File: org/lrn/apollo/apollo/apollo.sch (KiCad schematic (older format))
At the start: 2 parts, among them U1 74HC595, U2 5461AS-1

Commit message: apollo pcb
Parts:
- added J1, J2, J3, J4, J_CLK1, J_CLR1, J_GND1, J_OE1, J_SER1, J_VCC1: Conn_01x01_Male, Connector_Pin:Pin_D0.7mm_L6.5mm_W1.8mm_FlatFork, symbol Connector:Conn_01x01_Male
- added Q1, Q2, Q3, Q4: PN2222A, Package_TO_SOT_THT:TO-92_Inline, symbol Transistor_BJT:PN2222A
- added R1, R2, R3, R4, R5, R6, R7, R8: R, Resistor_THT:R_Axial_DIN0204_L3.6mm_D1.6mm_P5.08mm_Horizontal, symbol Device:R
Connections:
- net at U2.1 (es): now also R3.1; no longer U1.4 (QE)
- net at U2.10 (fs): now also R7.1; no longer U1.5 (QF)
- net at U2.11 (as): now also R1.1; no longer U1.15 (QA)
- net at U2.12 (d1): now also Q2.3 (C)
- net at U2.2 (ds): now also R6.1; no longer U1.3 (QD)
- net at U2.3 (dps): now also R8.1; no longer U1.7 (QH)
- net at U2.4 (cs): now also R2.1; no longer U1.2 (QC)
- net at U2.5 (gs): now also R4.1; no longer U1.6 (QG)
- net at U2.6 (d4): now also Q1.3 (C)
- net at U2.7 (bs): now also R5.1; no longer U1.1 (QB)
- net at U2.8 (d3): now also Q4.3 (C)
- net at U2.9 (d2): now also Q3.3 (C)
- net at U1.10 (~SRCLR): now also U1.16 (VCC), J_VCC1.1 (Pin_1)
- net at U1.11 (SRCLK): now also J_CLR1.1 (Pin_1)
- net at U1.12 (RCLK): now also J_CLK1.1 (Pin_1)
- net at U1.13 (~OE): now also J_OE1.1 (Pin_1)
- net at U1.14 (SER): now also J_SER1.1 (Pin_1)
- net at U1.8 (GND): now also J_GND1.1 (Pin_1), Q1.1 (E), Q2.1 (E), Q3.1 (E), Q4.1 (E)
- new net: R5.2, U1.1 (QB)
- new net: R1.2, U1.15 (QA)
- new net: R2.2, U1.2 (QC)
- new net: R6.2, U1.3 (QD)
- new net: R3.2, U1.4 (QE)
- new net: R7.2, U1.5 (QF)
- new net: R4.2, U1.6 (QG)
- new net: R8.2, U1.7 (QH)
- new net: J2.1 (Pin_1), Q2.2 (B)
- new net: J3.1 (Pin_1), Q3.2 (B)
- new net: J4.1 (Pin_1), Q4.2 (B)
- new net: J1.1 (Pin_1), Q1.2 (B)
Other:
- moved on the sheet: U1, U2

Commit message: apollo pcb fix: wrong transistor footprint
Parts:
- Q1, Q2, Q3, Q4: footprint Package_TO_SOT_THT:TO-92_Inline -> Package_TO_SOT_THT:TO-92_Wide
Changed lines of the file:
@@
 F 0 "Q2" H 5390 2096 50  0000 L CNN
 F 1 "PN2222A" H 5390 2005 50  0000 L CNN
-F 2 "Package_TO_SOT_THT:TO-92_Inline" H 5400 1975 50  0001 L CIN
+F 2 "Package_TO_SOT_THT:TO-92_Wide" H 5400 1975 50  0001 L CIN
 F 3 "http://www.fairchildsemi.com/ds/PN/PN2222A.pdf" H 5200 2050 50  0001 L CNN
 	1    5200 2050
@@
 F 0 "Q3" H 5740 2696 50  0000 L CNN
 F 1 "PN2222A" H 5740 2605 50  0000 L CNN
-F 2 "Package_TO_SOT_THT:TO-92_Inline" H 5750 2575 50  0001 L CIN
+F 2 "Package_TO_SOT_THT:TO-92_Wide" H 5750 2575 50  0001 L CIN
 F 3 "http://www.fairchildsemi.com/ds/PN/PN2222A.pdf" H 5550 2650 50  0001 L CNN
 	1    5550 2650
@@
 F 0 "Q4" H 6090 3196 50  0000 L CNN
 F 1 "PN2222A" H 6090 3105 50  0000 L CNN
-F 2 "Package_TO_SOT_THT:TO-92_Inline" H 6100 3075 50  0001 L CIN
+F 2 "Package_TO_SOT_THT:TO-92_Wide" H 6100 3075 50  0001 L CIN
 F 3 "http://www.fairchildsemi.com/ds/PN/PN2222A.pdf" H 5900 3150 50  0001 L CNN
 	1    5900 3150
@@
 F 0 "Q1" H 5040 1546 50  0000 L CNN
 F 1 "PN2222A" H 5040 1455 50  0000 L CNN
-F 2 "Package_TO_SOT_THT:TO-92_Inline" H 5050 1425 50  0001 L CIN
+F 2 "Package_TO_SOT_THT:TO-92_Wide" H 5050 1425 50  0001 L CIN
 F 3 "http://www.fairchildsemi.com/ds/PN/PN2222A.pdf" H 4850 1500 50  0001 L CNN
 	1    4850 1500

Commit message: apollo: new pcb
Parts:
- added Rb1, Rb2, Rb3, Rb4: R, apollo:R__Horizontal, symbol Device:R
- Q1, Q2, Q3, Q4: footprint Package_TO_SOT_THT:TO-92_Wide -> apollo:2N222A-TO-92_Wide
- R1, R2, R3, R4, R5, R6, R7, R8: footprint Resistor_THT:R_Axial_DIN0204_L3.6mm_D1.6mm_P5.08mm_Horizontal -> apollo:R__Horizontal
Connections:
- net VCC: now reaches J_VCC1.1 (Pin_1), U1.10 (~SRCLR), U1.16 (VCC)
- net GND: now reaches J_GND1.1 (Pin_1), Q1.1 (E), Q2.1 (E), Q3.1 (E), Q4.1 (E), U1.8 (GND)
- net at Q2.2 (B): now also Rb2.1; no longer J2.1 (Pin_1)
- net at Q3.2 (B): now also Rb3.1; no longer J3.1 (Pin_1)
- net at Q4.2 (B): now also Rb4.1; no longer J4.1 (Pin_1)
- net at Q1.2 (B): now also Rb1.1; no longer J1.1 (Pin_1)
- new net: J4.1 (Pin_1), Rb4.2
- new net: J3.1 (Pin_1), Rb3.2
- new net: J2.1 (Pin_1), Rb2.2
- new net: J1.1 (Pin_1), Rb1.2
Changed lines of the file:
@@
 F 0 "R7" V 4400 5050 50  0000 C CNN
 F 1 "R" V 4400 4950 50  0000 C CNN
-F 2 "Resistor_THT:R_Axial_DIN0204_L3.6mm_D1.6mm_P5.08mm_Horizontal" V 4330 5000 50  0001 C CNN
+F 2 "apollo:R__Horizontal" V 4330 5000 50  0001 C CNN
 F 3 "~" H 4400 5000 50  0001 C CNN
 	1    4400 5000
@@
 F 0 "R5" V 4400 4650 50  0000 C CNN
 F 1 "R" V 4400 4550 50  0000 C CNN
-F 2 "Resistor_THT:R_Axial_DIN0204_L3.6mm_D1.6mm_P5.08mm_Horizontal" V 4330 4600 50  0001 C CNN
+F 2 "apollo:R__Horizontal" V 4330 4600 50  0001 C CNN
 F 3 "~" H 4400 4600 50  0001 C CNN
 	1    4400 4600
@@
 F 0 "R2" V 4150 4750 50  0000 C CNN
 F 1 "R" V 4150 4650 50  0000 C CNN
-F 2 "Resistor_THT:R_Axial_DIN0204_L3.6mm_D1.6mm_P5.08mm_Horizontal" V 4080 4700 50  0001 C CNN
+F 2 "apollo:R__Horizontal" V 4080 4700 50  0001 C CNN
 F 3 "~" H 4150 4700 50  0001 C CNN
 	1    4150 4700
@@
 F 0 "R1" V 4150 4550 50  0000 C CNN
 F 1 "R" V 4150 4450 50  0000 C CNN
-F 2 "Resistor_THT:R_Axial_DIN0204_L3.6mm_D1.6mm_P5.08mm_Horizontal" V 4080 4500 50  0001 C CNN
+F 2 "apollo:R__Horizontal" V 4080 4500 50  0001 C CNN
 F 3 "~" H 4150 4500 50  0001 C CNN
 	1    4150 4500
@@
 F 0 "R6" V 4400 4850 50  0000 C CNN
 F 1 "R" V 4400 4750 50  0000 C CNN
-F 2 "Resistor_THT:R_Axial_DIN0204_L3.6mm_D1.6mm_P5.08mm_Horizontal" V 4330 4800 50  0001 C CNN
+F 2 "apollo:R__Horizontal" V 4330 4800 50  0001 C CNN
 F 3 "~" H 4400 4800 50  0001 C CNN
 	1    4400 4800
@@
 F 0 "R3" V 4150 4950 50  0000 C CNN
 F 1 "R" V 4150 4850 50  0000 C CNN
-F 2 "Resistor_THT:R_Axial_DIN0204_L3.6mm_D1.6mm_P5.08mm_Horizontal" V 4080 4900 50  0001 C CNN
+F 2 "apollo:R__Horizontal" V 4080 4900 50  0001 C CNN
 F 3 "~" H 4150 4900 50  0001 C CNN
 	1    4150 4900
@@
 F 0 "R4" V 4150 5150 50  0000 C CNN
 F 1 "R" V 4150 5050 50  0000 C CNN
-F 2 "Resistor_THT:R_Axial_DIN0204_L3.6mm_D1.6mm_P5.08mm_Horizontal" V 4080 5100 50  0001 C CNN
+F 2 "apollo:R__Horizontal" V 4080 5100 50  0001 C CNN
 F 3 "~" H 4150 5100 50  0001 C CNN
 	1    4150 5100
@@
 F 0 "R8" V 4400 5250 50  0000 C CNN
 F 1 "R" V 4400 5150 50  0000 C CNN
-F 2 "Resistor_THT:R_Axial_DIN0204_L3.6mm_D1.6mm_P5.08mm_Horizontal" V 4330 5200 50  0001 C CNN
+F 2 "apollo:R__Horizontal" V 4330 5200 50  0001 C CNN
 F 3 "~" H 4400 5200 50  0001 C CNN
 	1    4400 5200
@@
 F 0 "Q2" H 5390 2096 50  0000 L CNN
 F 1 "PN2222A" H 5390 2005 50  0000 L CNN
-F 2 "Package_TO_SOT_THT:TO-92_Wide" H 5400 1975 50  0001 L CIN
+F 2 "apollo:2N222A-TO-92_Wide" H 5400 1975 50  0001 L CIN
 F 3 "http://www.fairchildsemi.com/ds/PN/PN2222A.pdf" H 5200 2050 50  0001 L CNN
 	1    5200 2050
@@
 F 0 "Q3" H 5740 2696 50  0000 L CNN
 F 1 "PN2222A" H 5740 2605 50  0000 L CNN
-F 2 "Package_TO_SOT_THT:TO-92_Wide" H 5750 2575 50  0001 L CIN
+F 2 "apollo:2N222A-TO-92_Wide" H 5750 2575 50  0001 L CIN
 F 3 "http://www.fairchildsemi.com/ds/PN/PN2222A.pdf" H 5550 2650 50  0001 L CNN
 	1    5550 2650
@@
 F 0 "Q4" H 6090 3196 50  0000 L CNN
 F 1 "PN2222A" H 6090 3105 50  0000 L CNN
-F 2 "Package_TO_SOT_THT:TO-92_Wide" H 6100 3075 50  0001 L CIN
+F 2 "apollo:2N222A-TO-92_Wide" H 6100 3075 50  0001 L CIN
 F 3 "http://www.fairchildsemi.com/ds/PN/PN2222A.pdf" H 5900 3150 50  0001 L CNN
 	1    5900 3150
@@
 F 0 "Q1" H 5040 1546 50  0000 L CNN
 F 1 "PN2222A" H 5040 1455 50  0000 L CNN
-F 2 "Package_TO_SOT_THT:TO-92_Wide" H 5050 1425 50  0001 L CIN
+F 2 "apollo:2N222A-TO-92_Wide" H 5050 1425 50  0001 L CIN
 F 3 "http://www.fairchildsemi.com/ds/PN/PN2222A.pdf" H 4850 1500 50  0001 L CNN
 	1    4850 1500
@@
 	1    0    0    -1
 $EndComp
-Wire Wire Line
-	5350 2650 2750 2650
 $Comp
 L Connector:Conn_01x01_Male J2
@@
 	1    0    0    -1
 $EndComp
-Wire Wire Line
-	2750 2050 5000 2050
 $Comp
 L Connector:Conn_01x01_Male J1
@@
 	1    0    0    -1
 $EndComp
-Wire Wire Line
-	2750 1500 4650 1500
 Connection ~ 4150 3700
 Wire Wire Line
@@
 $EndComp
 Wire Wire Line
-	5700 3150 2750 3150
-Wire Wire Line
 	2750 5000 3100 5000
 Wire Wire Line
 	5600 3800 5600 4400
+$Comp
+L Device:R Rb1
+U 1 1 5F5EB03E
+P 3750 1500
+F 0 "Rb1" V 3543 1500 50  0000 C CNN
+F 1 "R" V 3634 1500 50  0000 C CNN
+F 2 "apollo:R__Horizontal" V 3680 1500 50  0001 C CNN
+F 3 "~" H 3750 1500 50  0001 C CNN
+	1    3750 1500
+	0    1    1    0
+$EndComp
+$Comp
+L Device:R Rb2
+U 1 1 5F5EB7B3
+P 3750 2050
+F 0 "Rb2" V 3543 2050 50  0000 C CNN
+F 1 "R" V 3634 2050 50  0000 C CNN
+F 2 "apollo:R__Horizontal" V 3680 2050 50  0001 C CNN
+F 3 "~" H 3750 2050 50  0001 C CNN
+	1    3750 2050
+	0    1    1    0
+$EndComp
+$Comp
+L Device:R Rb3
+U 1 1 5F5EBD6A
+P 3750 2650
+F 0 "Rb3" V 3543 2650 50  0000 C CNN
+F 1 "R" V 3634 2650 50  0000 C CNN
+F 2 "apollo:R__Horizontal" V 3680 2650 50  0001 C CNN
+F 3 "~" H 3750 2650 50  0001 C CNN
+	1    3750 2650
+	0    1    1    0
+$EndComp
+$Comp
+L Device:R Rb4
+U 1 1 5F5EC2EE
+P 3750 3150
+F 0 "Rb4" V 3543 3150 50  0000 C CNN
+F 1 "R" V 3634 3150 50  0000 C CNN
+F 2 "apollo:R__Horizontal" V 3680 3150 50  0001 C CNN
+F 3 "~" H 3750 3150 50  0001 C CNN
+	1    3750 3150
+	0    1    1    0
+$EndComp
+Wire Wire Line
+	2750 3150 3600 3150
+Wire Wire Line
+	2750 2650 3600 2650
+Wire Wire Line
+	2750 2050 3600 2050
+Wire Wire Line
+	2750 1500 3600 1500
+Wire Wire Line
+	3900 1500 4650 1500
+Wire Wire Line
+	3900 2050 5000 2050
+Wire Wire Line
+	3900 2650 5350 2650
+Wire Wire Line
+	3900 3150 5700 3150
+$Comp
+L power:VCC #PWR0101
+U 1 1 5F60A86A
+P 2950 4000
+F 0 "#PWR0101" H 2950 3850 50  0001 C CNN
+F 1 "VCC" H 2967 4173 50  0000 C CNN
+F 2 "" H 2950 4000 50  0001 C CNN
+F 3 "" H 2950 4000 50  0001 C CNN
+	1    2950 4000
+	1    0    0    -1
+$EndComp
+Wire Wire Line
+	2950 4000 2950 4150
+$Comp
+L power:GND #PWR0102
+U 1 1 5F60E32A
+P 3500 6050
+F 0 "#PWR0102" H 3500 5800 50  0001 C CNN
+F 1 "GND" H 3505 5877 50  0000 C CNN
+F 2 "" H 3500 6050 50  0001 C CNN
+F 3 "" H 3500 6050 50  0001 C CNN
+	1    3500 6050
+	1    0    0    -1
+$EndComp
+Wire Wire Line
+	3500 6050 3500 5850
+Connection ~ 3500 5850
+Connection ~ 2950 4000
+Connection ~ 3500 5600
 $EndSCHEMATC

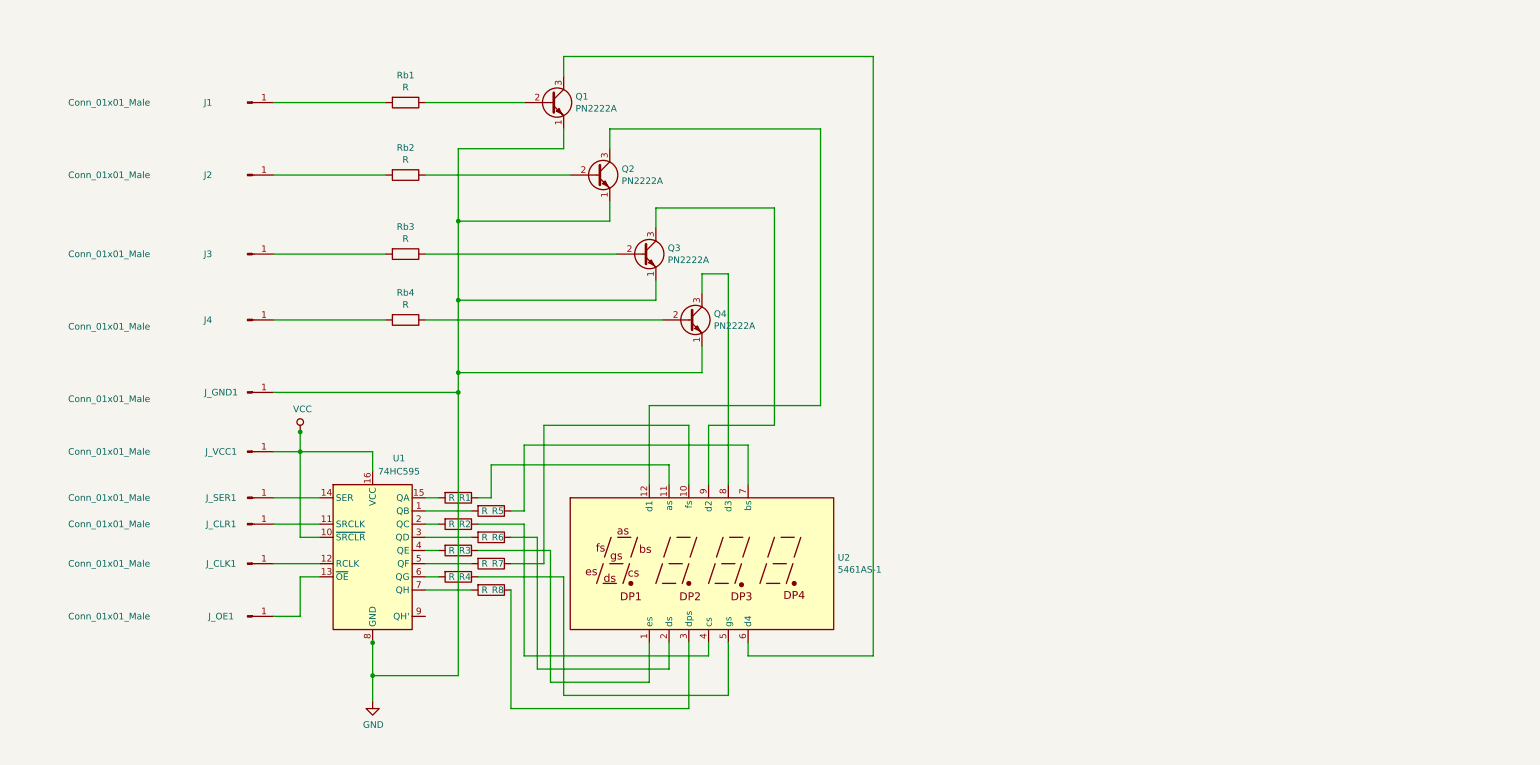
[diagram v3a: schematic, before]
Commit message: apollo: schematic for keyb shift register
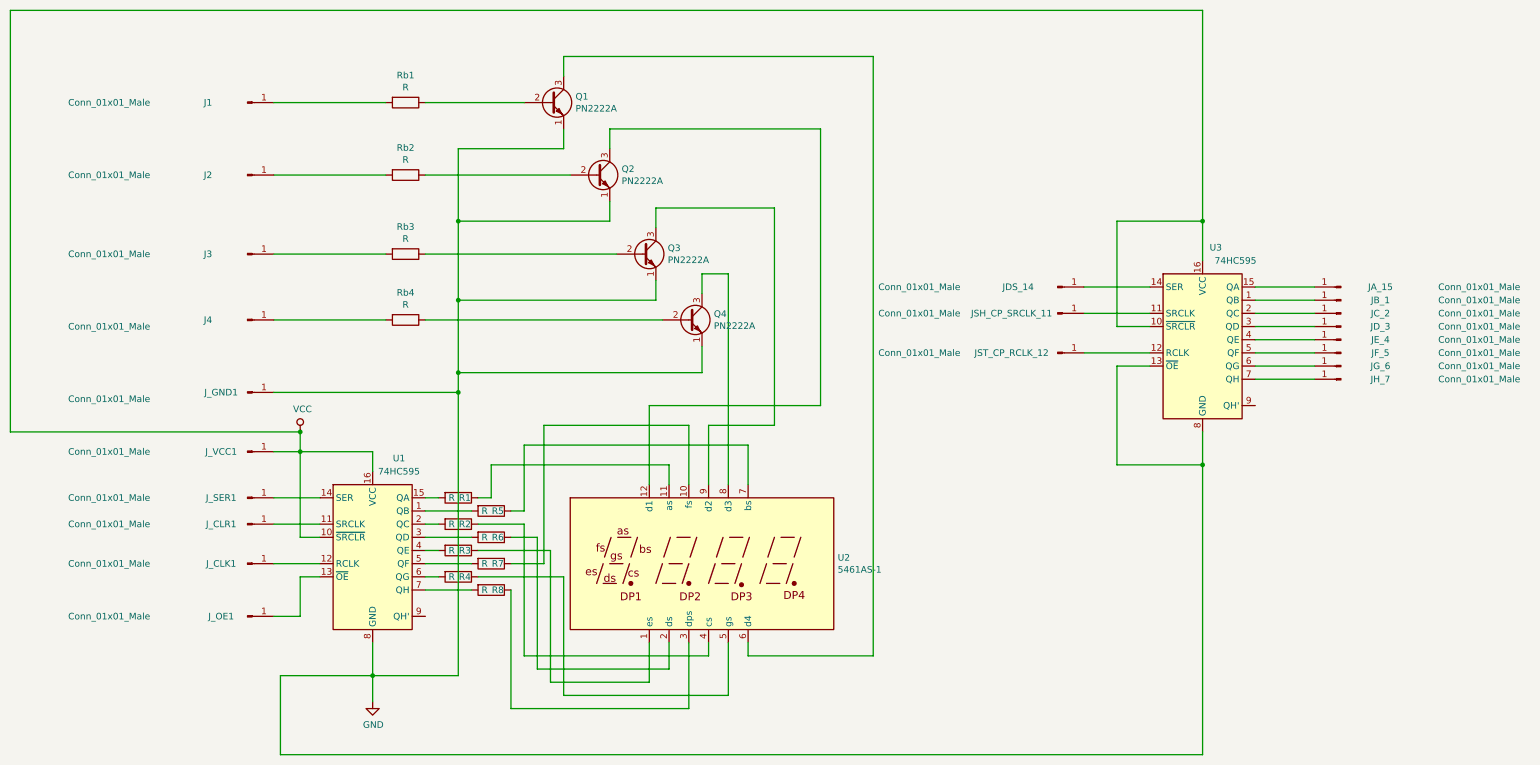
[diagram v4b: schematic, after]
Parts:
- added JA_15, JB_1, JC_2, JDS_14, JD_3, JE_4, JF_5, JG_6, JH_7, JSH_CP_SRCLK_11, JST_CP_RCLK_12: Conn_01x01_Male, Connector_Pin:Pin_D0.7mm_L6.5mm_W1.8mm_FlatFork, symbol Connector:Conn_01x01_Male
- added U3: 74HC595, Package_DIP:DIP-16_W7.62mm_LongPads, symbol 74xx:74HC595
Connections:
- net GND: now also U3.13 (~OE), U3.8 (GND)
- net VCC: now also U3.10 (~SRCLR), U3.16 (VCC)
- new net: JB_1.1 (Pin_1), U3.1 (QB)
- new net: JSH_CP_SRCLK_11.1 (Pin_1), U3.11 (SRCLK)
- new net: JST_CP_RCLK_12.1 (Pin_1), U3.12 (RCLK)
- new net: JDS_14.1 (Pin_1), U3.14 (SER)
- new net: JA_15.1 (Pin_1), U3.15 (QA)
- new net: JC_2.1 (Pin_1), U3.2 (QC)
- new net: JD_3.1 (Pin_1), U3.3 (QD)
- new net: JE_4.1 (Pin_1), U3.4 (QE)
- new net: JF_5.1 (Pin_1), U3.5 (QF)
- new net: JG_6.1 (Pin_1), U3.6 (QG)
- new net: JH_7.1 (Pin_1), U3.7 (QH)
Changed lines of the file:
@@
 	3500 6050 3500 5850
 Connection ~ 3500 5850
+$Comp
+L 74xx:74HC595 U3
+U 1 1 5F575A47
+P 9800 3300
+F 0 "U3" H 9900 4000 50  0000 C CNN
+F 1 "74HC595" H 10050 3900 50  0000 C CNN
+F 2 "Package_DIP:DIP-16_W7.62mm_LongPads" H 9800 3300 50  0001 C CNN
+F 3 "http://www.ti.com/lit/ds/symlink/sn74hc595.pdf" H 9800 3300 50  0001 C CNN
+	1    9800 3300
+	1    0    0    -1
+$EndComp
+$Comp
+L Connector:Conn_01x01_Male JB_1
+U 1 1 5F5880D1
+P 10850 3000
+F 0 "JB_1" H 10550 3000 50  0000 C CNN
+F 1 "Conn_01x01_Male" H 9800 3000 50  0000 C CNN
+F 2 "Connector_Pin:Pin_D0.7mm_L6.5mm_W1.8mm_FlatFork" H 10850 3000 50  0001 C CNN
+F 3 "~" H 10850 3000 50  0001 C CNN
+	1    10850 3000
+	-1   0    0    1
+$EndComp
+$Comp
+L Connector:Conn_01x01_Male JA_15
+U 1 1 5F580A07
+P 10850 2900
+F 0 "JA_15" H 10550 2900 50  0000 C CNN
+F 1 "Conn_01x01_Male" H 9800 2900 50  0000 C CNN
+F 2 "Connector_Pin:Pin_D0.7mm_L6.5mm_W1.8mm_FlatFork" H 10850 2900 50  0001 C CNN
+F 3 "~" H 10850 2900 50  0001 C CNN
+	1    10850 2900
+	-1   0    0    1
+$EndComp
+$Comp
+L Connector:Conn_01x01_Male JC_2
+U 1 1 5F58E8BB
+P 10850 3100
+F 0 "JC_2" H 10550 3100 50  0000 C CNN
+F 1 "Conn_01x01_Male" H 9800 3100 50  0000 C CNN
+F 2 "Connector_Pin:Pin_D0.7mm_L6.5mm_W1.8mm_FlatFork" H 10850 3100 50  0001 C CNN
+F 3 "~" H 10850 3100 50  0001 C CNN
+	1    10850 3100
+	-1   0    0    1
+$EndComp
+$Comp
+L Connector:Conn_01x01_Male JD_3
+U 1 1 5F5915FD
+P 10850 3200
+F 0 "JD_3" H 10550 3200 50  0000 C CNN
+F 1 "Conn_01x01_Male" H 9800 3200 50  0000 C CNN
+F 2 "Connector_Pin:Pin_D0.7mm_L6.5mm_W1.8mm_FlatFork" H 10850 3200 50  0001 C CNN
+F 3 "~" H 10850 3200 50  0001 C CNN
+	1    10850 3200
+	-1   0    0    1
+$EndComp
+$Comp
+L Connector:Conn_01x01_Male JE_4
+U 1 1 5F5944F8
+P 10850 3300
+F 0 "JE_4" H 10550 3300 50  0000 C CNN
+F 1 "Conn_01x01_Male" H 9800 3300 50  0000 C CNN
+F 2 "Connector_Pin:Pin_D0.7mm_L6.5mm_W1.8mm_FlatFork" H 10850 3300 50  0001 C CNN
+F 3 "~" H 10850 3300 50  0001 C CNN
+	1    10850 3300
+	-1   0    0    1
+$EndComp
+$Comp
+L Connector:Conn_01x01_Male JF_5
+U 1 1 5F5974B0
+P 10850 3400
+F 0 "JF_5" H 10550 3400 50  0000 C CNN
+F 1 "Conn_01x01_Male" H 9800 3400 50  0000 C CNN
+F 2 "Connector_Pin:Pin_D0.7mm_L6.5mm_W1.8mm_FlatFork" H 10850 3400 50  0001 C CNN
+F 3 "~" H 10850 3400 50  0001 C CNN
+	1    10850 3400
+	-1   0    0    1
+$EndComp
+$Comp
+L Connector:Conn_01x01_Male JG_6
+U 1 1 5F59A202
+P 10850 3500
+F 0 "JG_6" H 10550 3500 50  0000 C CNN
+F 1 "Conn_01x01_Male" H 9800 3500 50  0000 C CNN
+F 2 "Connector_Pin:Pin_D0.7mm_L6.5mm_W1.8mm_FlatFork" H 10850 3500 50  0001 C CNN
+F 3 "~" H 10850 3500 50  0001 C CNN
+	1    10850 3500
+	-1   0    0    1
+$EndComp
+$Comp
+L Connector:Conn_01x01_Male JH_7
+U 1 1 5F59CEC9
+P 10850 3600
+F 0 "JH_7" H 10550 3600 50  0000 C CNN
+F 1 "Conn_01x01_Male" H 9800 3600 50  0000 C CNN
+F 2 "Connector_Pin:Pin_D0.7mm_L6.5mm_W1.8mm_FlatFork" H 10850 3600 50  0001 C CNN
+F 3 "~" H 10850 3600 50  0001 C CNN
+	1    10850 3600
+	-1   0    0    1
+$EndComp
+Wire Wire Line
+	10200 2900 10650 2900
+Wire Wire Line
+	10200 3000 10650 3000
+Wire Wire Line
+	10200 3100 10650 3100
+Wire Wire Line
+	10200 3200 10650 3200
+Wire Wire Line
+	10200 3300 10650 3300
+Wire Wire Line
+	10200 3400 10650 3400
+Wire Wire Line
+	10200 3500 10650 3500
+Wire Wire Line
+	10200 3600 10650 3600
+Wire Wire Line
+	3500 5850 2800 5850
+Wire Wire Line
+	2800 5850 2800 6450
+Wire Wire Line
+	2800 6450 9800 6450
+Wire Wire Line
+	9800 6450 9800 4250
+Wire Wire Line
+	9400 3500 9150 3500
+Wire Wire Line
+	9150 3500 9150 4250
+Wire Wire Line
+	9150 4250 9800 4250
+Connection ~ 9800 4250
+Wire Wire Line
+	9800 4250 9800 4000
+Wire Wire Line
+	2950 4000 750  4000
+Wire Wire Line
+	750  4000 750  800
+Wire Wire Line
+	750  800  9800 800
+Wire Wire Line
+	9800 800  9800 2400
 Connection ~ 2950 4000
-Connection ~ 3500 5600
+Wire Wire Line
+	9400 3200 9150 3200
+Wire Wire Line
+	9150 3200 9150 2400
+Wire Wire Line
+	9150 2400 9800 2400
+Connection ~ 9800 2400
+Wire Wire Line
+	9800 2400 9800 2700
+$Comp
+L Connector:Conn_01x01_Male JDS_14
+U 1 1 5F5E2288
+P 8700 2900
+F 0 "JDS_14" H 8400 2900 50  0000 C CNN
+F 1 "Conn_01x01_Male" H 7650 2900 50  0000 C CNN
+F 2 "Connector_Pin:Pin_D0.7mm_L6.5mm_W1.8mm_FlatFork" H 8700 2900 50  0001 C CNN
+F 3 "~" H 8700 2900 50  0001 C CNN
+	1    8700 2900
+	1    0    0    -1
+$EndComp
+Wire Wire Line
+	8900 2900 9400 2900
+$Comp
+L Connector:Conn_01x01_Male JST_CP_RCLK_12
+U 1 1 5F5F78E6
+P 8700 3400
+F 0 "JST_CP_RCLK_12" H 8350 3400 50  0000 C CNN
+F 1 "Conn_01x01_Male" H 7650 3400 50  0000 C CNN
+F 2 "Connector_Pin:Pin_D0.7mm_L6.5mm_W1.8mm_FlatFork" H 8700 3400 50  0001 C CNN
+F 3 "~" H 8700 3400 50  0001 C CNN
+	1    8700 3400
+	1    0    0    -1
+$EndComp
+Wire Wire Line
+	8900 3400 9400 3400
+$Comp
+L Connector:Conn_01x01_Male JSH_CP_SRCLK_11
+U 1 1 5F60047B
+P 8700 3100
+F 0 "JSH_CP_SRCLK_11" H 8350 3100 50  0000 C CNN
+F 1 "Conn_01x01_Male" H 7650 3100 50  0000 C CNN
+F 2 "Connector_Pin:Pin_D0.7mm_L6.5mm_W1.8mm_FlatFork" H 8700 3100 50  0001 C CNN
+F 3 "~" H 8700 3100 50  0001 C CNN
+	1    8700 3100
+	1    0    0    -1
+$EndComp
+Wire Wire Line
+	8900 3100 9400 3100
 $EndSCHEMATC
